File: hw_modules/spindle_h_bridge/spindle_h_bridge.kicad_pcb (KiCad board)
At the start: 2 copper layers, 86.4 x 68.6 mm, 66 parts, among them J1 SIGNAL, J2 MOTOR, J3 POWER, J4 POWER, Q1 IRG4PH40U, Q2 IRG4PH40U, Q3 IRG4PH40U, Q4 IRG4PH40U, U1 ADuM1200AR, U2 LM1117-5.0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

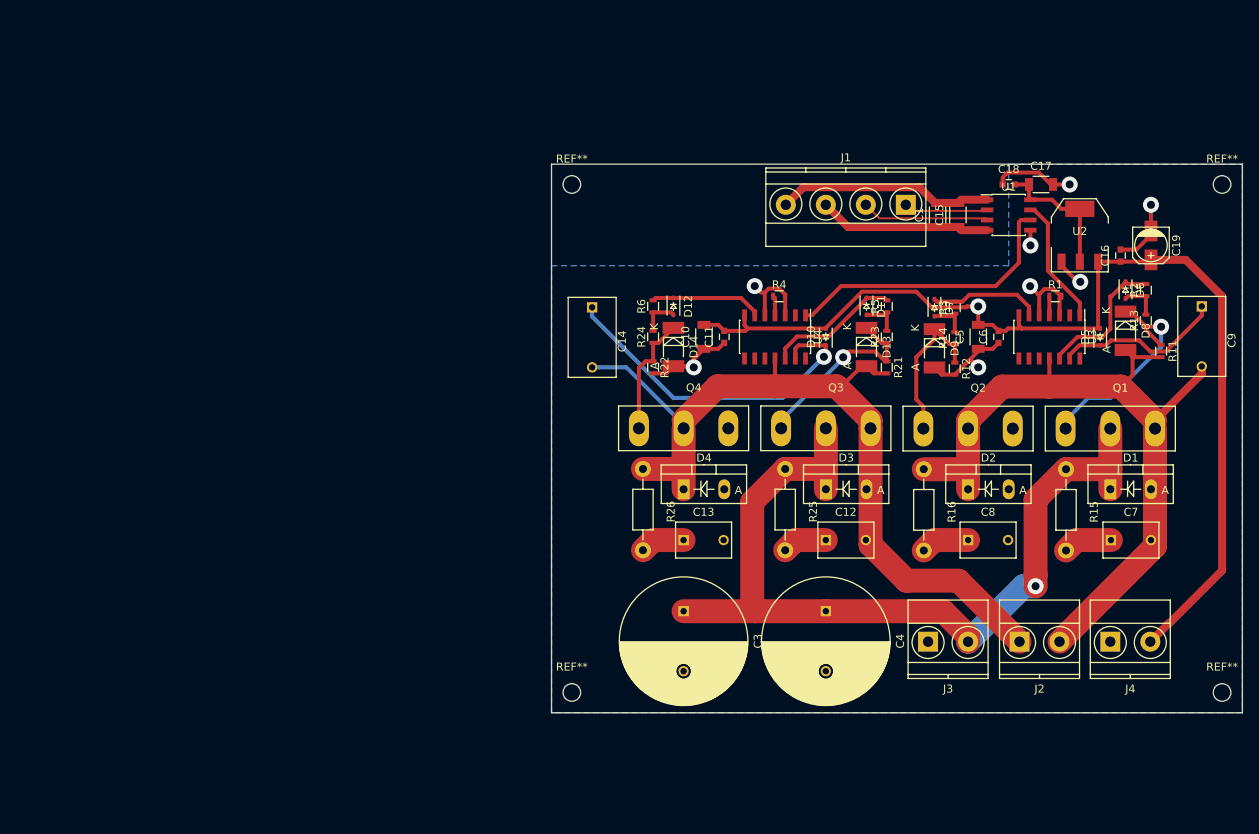
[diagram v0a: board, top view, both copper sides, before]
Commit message: Add PWM to -+10V board
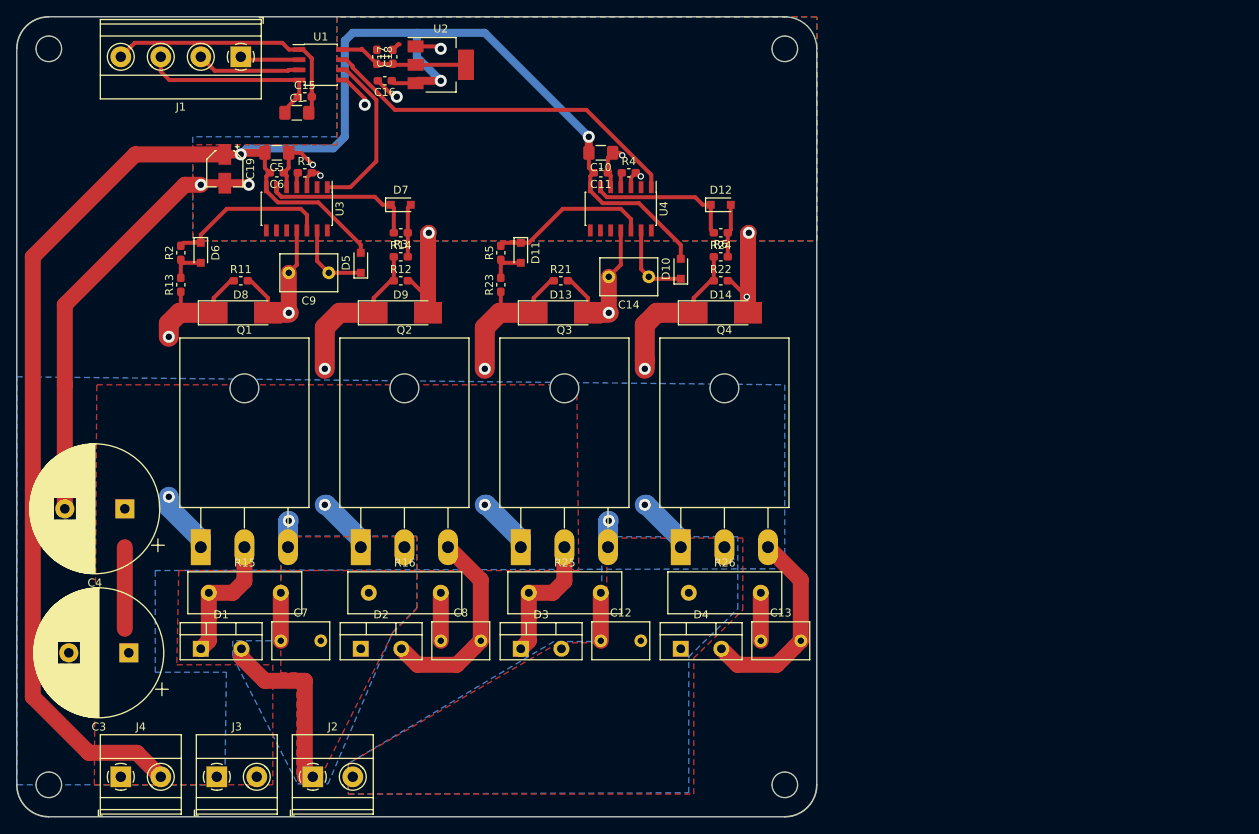
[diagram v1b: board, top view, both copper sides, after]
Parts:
- removed REF** (x4): MountingHole_2.2mm_M2, Mounting_Holes:MountingHole_2.2mm_M2
- added H1: MountingHole, MountingHole:MountingHole_3.2mm_M3, F.Cu at (146.0, 44.0)
- added H2: MountingHole, MountingHole:MountingHole_3.2mm_M3, F.Cu at (146.0, 136.0)
- added H3: MountingHole, MountingHole:MountingHole_3.2mm_M3, F.Cu at (54.0, 44.0)
- added H4: MountingHole, MountingHole:MountingHole_3.2mm_M3, F.Cu at (54.0, 136.0)
- C1, C10, C5: footprint Capacitors_SMD:C_1206 -> Capacitor_SMD:C_1206_3216Metric_Pad1.42x1.75mm_HandSolder
- C11, C16, C18, C6: footprint Capacitors_SMD:C_0603 -> Capacitor_SMD:C_0603_1608Metric_Pad1.05x0.95mm_HandSolder
- C12, C13, C7, C8: footprint Capacitors_ThroughHole:C_Rect_L7_W4.5_P5 -> Capacitor_THT:C_Rect_L7.0mm_W4.5mm_P5.00mm
- C14, C9: footprint Capacitors_ThroughHole:C_Rect_L10_W6_P7.5 -> Capacitor_THT:C_Rect_L7.0mm_W4.5mm_P5.00mm
- C15, C17: footprint Capacitors_SMD:C_1206 -> Capacitor_SMD:C_0603_1608Metric_Pad1.05x0.95mm_HandSolder
- C19: footprint Capacitors_SMD:c_elec_4x4.5 -> Capacitor_SMD:CP_Elec_4x4.5
- C3, C4: footprint Capacitors_ThroughHole:C_Radial_D16_L25_P7.5 -> Capacitor_THT:CP_Radial_D16.0mm_P7.50mm
- D1, D2, D3, D4: footprint Diodes_ThroughHole:Diode_TO-220_Vertical -> Package_TO_SOT_THT:TO-220-2_Vertical
- D10, D11, D12, D5, D6, D7: footprint Diodes_SMD:SOD-323 -> Diode_SMD:D_SOD-323_HandSoldering
- D13, D14, D8, D9: footprint Diodes_SMD:MELF_Standard -> Diode_SMD:D_MELF_Handsoldering
- J1: footprint Terminal_Blocks:TerminalBlock_Pheonix_MKDS1.5-4pol -> TerminalBlock_Phoenix:TerminalBlock_Phoenix_MKDS-1,5-4_1x04_P5.00mm_Horizontal
- J2, J3, J4: footprint Terminal_Blocks:TerminalBlock_Pheonix_MKDS1.5-2pol -> TerminalBlock_Phoenix:TerminalBlock_Phoenix_MKDS-1,5-2_1x02_P5.00mm_Horizontal
- Q1, Q2, Q3, Q4: footprint TO_SOT_Packages_THT:TO-247_Vertical_Neutral123 -> Package_TO_SOT_THT:TO-247-3_Horizontal_TabDown
- R1, R11, R12, R13, R14, R2, R21, R22, R23, R24, R3, R4, R5, R6: footprint Resistors_SMD:R_0603 -> Resistor_SMD:R_0603_1608Metric_Pad1.05x0.95mm_HandSolder
- R15, R16, R25, R26: footprint Resistors_ThroughHole:Resistor_Horizontal_RM10mm -> Resistor_THT:R_Box_L14.0mm_W5.0mm_P9.00mm
- U1: footprint Housings_SOIC:SOIC-8_3.9x4.9mm_Pitch1.27mm -> Package_SO:SOIC-8_3.9x4.9mm_P1.27mm
- U2: footprint TO_SOT_Packages_SMD:SOT-223 -> Package_TO_SOT_SMD:SOT-223
- U3, U4: footprint Housings_SOIC:SOIC-14_3.9x8.7mm_Pitch1.27mm -> Package_SO:SOIC-14_3.9x8.7mm_P1.27mm
- moved J4 124.8 mm to (63.0, 135.0)
- moved R2 120.7 mm to (70.5, 69.5)
- moved R13 120.7 mm to (70.5, 73.5)
- moved C19 116.2 mm to (76.0, 59.0)
- moved D6 115.7 mm to (73.0, 69.5)
- moved D1 115.4 mm to (73.0, 119.0)
- moved R11 115.4 mm to (78.0, 73.0), turned to 0 degrees
- moved Q1 114.7 mm to (73.0, 106.3)
- moved D8 110.6 mm to (78.0, 77.0), turned to 0 degrees
- moved C9 109.2 mm to (89.0, 72.0), turned to 180 degrees
- moved R15 108.3 mm to (74.0, 112.0), turned to 0 degrees
- moved C7 104.5 mm to (83.0, 118.0)
- moved U3 95.4 mm to (85.0, 64.0)
- moved R1 95.1 mm to (86.0, 59.5)
- moved C16 94.5 mm to (96.0, 48.0), turned to 180 degrees
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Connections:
- J2 pad 1: /right-half-bridge/OUT -> /left-half-bridge/OUT
- J2 pad 2: /left-half-bridge/OUT -> /right-half-bridge/OUT
- U1 pad 6: /right-half-bridge/PWM -> /left-half-bridge/PWM
- U1 pad 7: /left-half-bridge/PWM -> /right-half-bridge/PWM
- U3 pad 2: (no net) -> Net-(U3-Pad2)
- U4 pad 2: (no net) -> Net-(U4-Pad2)
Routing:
- net GND: track 69.0 -> 169.0 mm, vias 8 -> 12
- net +15V: track 132.0 -> 229.2 mm, vias 1 -> 3
- net VCC: track 110.5 -> 43.6 mm, vias 1 -> 0
- net /right-half-bridge/OUT: track 105.8 -> 49.4 mm, vias 0 -> 2
- net Net-(C14-Pad1): track 43.8 -> 10.3 mm, vias 1 -> 0
- net Net-(D14-Pad1): track 15.3 -> 44.8 mm, vias 0 -> 2
- net Net-(D9-Pad1): track 19.4 -> 44.6 mm, vias 0 -> 2
- net /left-half-bridge/OUT: track 95.4 -> 71.0 mm, vias 0 -> 2
- net Net-(D13-Pad1): track 24.0 -> 44.3 mm, vias 1 -> 2
- net Net-(D8-Pad1): track 27.6 -> 43.7 mm, vias 1 -> 2
- net Net-(C9-Pad1): track 21.3 -> 9.90 mm
- net /right-half-bridge/PWM: track 36.0 -> 46.2 mm
- net +5V: track 27.1 -> 32.4 mm
- net Net-(D7-Pad1): track 14.0 -> 19.2 mm
- net /left-half-bridge/PWM: track 16.0 -> 20.9 mm
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- added copper zone on B.Cu, net /left-half-bridge/OUT
- added copper zone on F.Cu, net /left-half-bridge/OUT
- added copper zone on B.Cu, net /right-half-bridge/OUT
- added copper zone on F.Cu, net /right-half-bridge/OUT
- added copper zone on F.Cu, net GND
- added copper zone on F.Cu, net VCC
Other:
- board size 86.4 x 68.6 mm -> 100 x 100 mm
- copper layers 2 -> 4
- net class Default: via_dia 0.6 -> 0.8
- rule pad_to_mask_clearance: 0.2 -> 0
